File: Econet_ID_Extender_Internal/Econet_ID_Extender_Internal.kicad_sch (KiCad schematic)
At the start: 3 parts, among them J1 Conn_01x03_Male, J2 Conn_02x08_Odd_Even, J3 Conn_02x06_Odd_Even

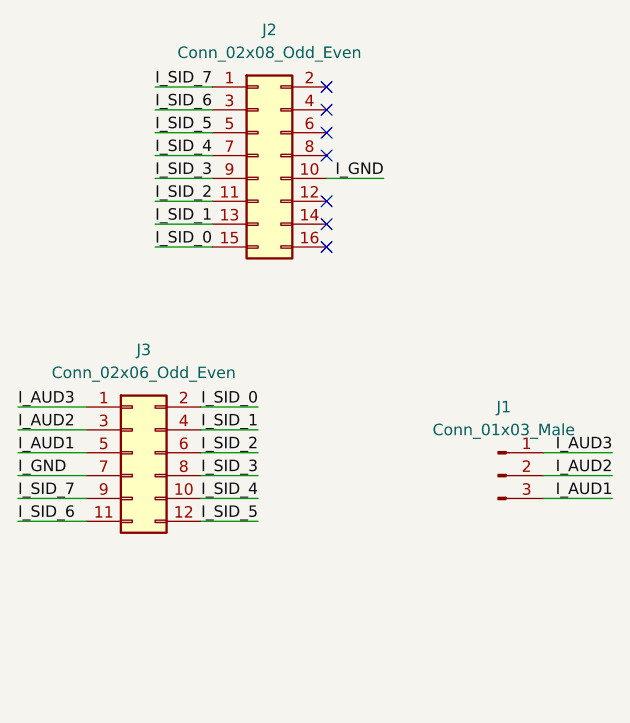
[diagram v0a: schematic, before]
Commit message: Swap to standard 2.54 pitch ribbon
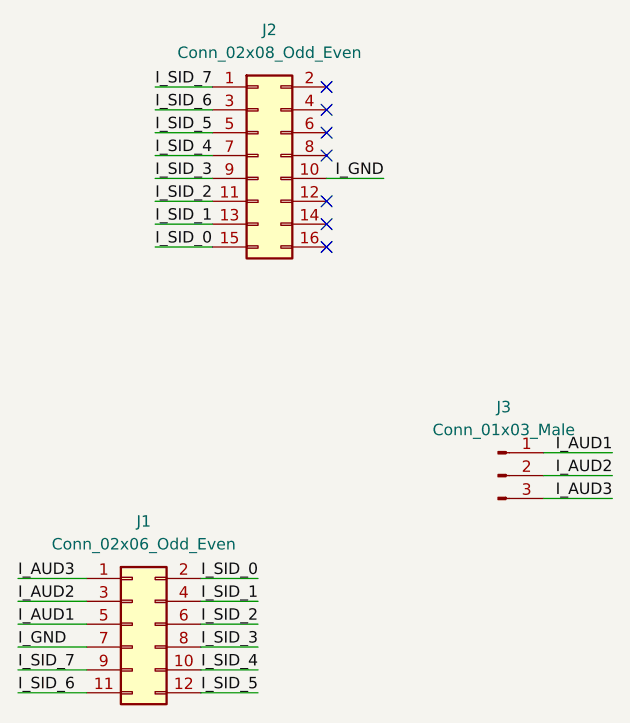
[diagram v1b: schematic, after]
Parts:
- removed J3: Conn_02x06_Odd_Even, AliExpress_Stuff:MicroMatch-12p-SMD, symbol Connector_Generic:Conn_02x06_Odd_Even
- added J1: Conn_02x06_Odd_Even, Connector_IDC:IDC-Header_2x06_P2.54mm_Vertical_SMD, symbol Connector_Generic:Conn_02x06_Odd_Even
- renumbered J1 to J3
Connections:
- net I_AUD1: now also J3.1 (Pin_1), J1.5 (Pin_5); no longer J3.3 (Pin_3)
- net I_AUD2: now also J1.3 (Pin_3)
- net I_AUD3: now also J3.3 (Pin_3), J1.1 (Pin_1); no longer J3.1 (Pin_1)
- net I_GND: now also J1.7 (Pin_7)
- net I_SID_0: now also J1.2 (Pin_2)
- net I_SID_1: now also J1.4 (Pin_4)
- net I_SID_2: now also J1.6 (Pin_6)
- net I_SID_3: now also J1.8 (Pin_8)
- net I_SID_4: now also J1.10 (Pin_10)
- net I_SID_5: now also J1.12 (Pin_12)
- net I_SID_6: now also J1.11 (Pin_11)
- net I_SID_7: now also J1.9 (Pin_9)
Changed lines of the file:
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@@
+    (stroke (width 0) (type default) (color 0 0 0 0))
+  )
+  (wire (pts (xy 124.46 121.92) (xy 130.81 121.92))
     (stroke (width 0) (type default) (color 0 0 0 0))
   )
@@
     (stroke (width 0) (type default) (color 0 0 0 0))
   )
-  (wire (pts (xy 124.46 105.41) (xy 130.81 105.41))
-    (stroke (width 0) (type default) (color 0 0 0 0))
-  )
-  (wire (pts (xy 124.46 110.49) (xy 130.81 110.49))
-    (stroke (width 0) (type default) (color 0 0 0 0))
-  )
-  (wire (pts (xy 124.46 115.57) (xy 130.81 115.57))
+  (wire (pts (xy 104.14 132.08) (xy 111.76 132.08))
+    (stroke (width 0) (type default) (color 0 0 0 0))
+  )
+  (wire (pts (xy 124.46 129.54) (xy 130.81 129.54))
     (stroke (width 0) (type default) (color 0 0 0 0))
   )
@@
     (stroke (width 0) (type default) (color 0 0 0 0))
   )
+  (wire (pts (xy 104.14 121.92) (xy 111.76 121.92))
+    (stroke (width 0) (type default) (color 0 0 0 0))
+  )
   (wire (pts (xy 162.56 107.95) (xy 170.18 107.95))
     (stroke (width 0) (type default) (color 0 0 0 0))
   )
-  (wire (pts (xy 104.14 115.57) (xy 111.76 115.57))
-    (stroke (width 0) (type default) (color 0 0 0 0))
-  )
   (wire (pts (xy 119.38 74.93) (xy 125.73 74.93))
     (stroke (width 0) (type default) (color 0 0 0 0))
@@
     (stroke (width 0) (type default) (color 0 0 0 0))
   )
-  (wire (pts (xy 104.14 113.03) (xy 111.76 113.03))
-    (stroke (width 0) (type default) (color 0 0 0 0))
-  )
-  (wire (pts (xy 124.46 102.87) (xy 130.81 102.87))
+  (wire (pts (xy 124.46 134.62) (xy 130.81 134.62))
+    (stroke (width 0) (type default) (color 0 0 0 0))
+  )
+  (wire (pts (xy 104.14 127) (xy 111.76 127))
+    (stroke (width 0) (type default) (color 0 0 0 0))
+  )
+  (wire (pts (xy 124.46 124.46) (xy 130.81 124.46))
     (stroke (width 0) (type default) (color 0 0 0 0))
   )
@@
     (stroke (width 0) (type default) (color 0 0 0 0))
   )
-  (wire (pts (xy 124.46 113.03) (xy 130.81 113.03))
-    (stroke (width 0) (type default) (color 0 0 0 0))
-  )
-  (wire (pts (xy 104.14 102.87) (xy 111.76 102.87))
-    (stroke (width 0) (type default) (color 0 0 0 0))
-  )
   (wire (pts (xy 119.38 69.85) (xy 125.73 69.85))
     (stroke (width 0) (type default) (color 0 0 0 0))
@@
     (stroke (width 0) (type default) (color 0 0 0 0))
   )
-  (wire (pts (xy 104.14 105.41) (xy 111.76 105.41))
-    (stroke (width 0) (type default) (color 0 0 0 0))
-  )
-  (wire (pts (xy 104.14 107.95) (xy 111.76 107.95))
-    (stroke (width 0) (type default) (color 0 0 0 0))
-  )
-  (wire (pts (xy 104.14 110.49) (xy 111.76 110.49))
-    (stroke (width 0) (type default) (color 0 0 0 0))
-  )
-  (wire (pts (xy 124.46 107.95) (xy 130.81 107.95))
-    (stroke (width 0) (type default) (color 0 0 0 0))
-  )
-  (label "I_SID_4" (at 130.81 113.03 180)
-    (effects (font (size 1.27 1.27)) (justify right bottom))
+  (wire (pts (xy 124.46 127) (xy 130.81 127))
+    (stroke (width 0) (type default) (color 0 0 0 0))
+  )
+  (wire (pts (xy 124.46 132.08) (xy 130.81 132.08))
+    (stroke (width 0) (type default) (color 0 0 0 0))
+  )
+  (wire (pts (xy 104.14 134.62) (xy 111.76 134.62))
+    (stroke (width 0) (type default) (color 0 0 0 0))
+  )
+  (wire (pts (xy 104.14 124.46) (xy 111.76 124.46))
+    (stroke (width 0) (type default) (color 0 0 0 0))
+  )
+  (wire (pts (xy 104.14 129.54) (xy 111.76 129.54))
+    (stroke (width 0) (type default) (color 0 0 0 0))
   )
   (label "I_AUD2" (at 170.18 110.49 180)
     (effects (font (size 1.27 1.27)) (justify right bottom))
   )
-  (label "I_SID_1" (at 130.81 105.41 180)
-    (effects (font (size 1.27 1.27)) (justify right bottom))
-  )
-  (label "I_GND" (at 104.14 110.49 0)
-    (effects (font (size 1.27 1.27)) (justify left bottom))
-  )
-  (label "I_AUD1" (at 104.14 107.95 0)
-    (effects (font (size 1.27 1.27)) (justify left bottom))
+  (label "I_AUD2" (at 104.14 124.46 0)
+    (effects (font (size 1.27 1.27)) (justify left bottom))
+  )
+  (label "I_SID_3" (at 130.81 129.54 180)
+    (effects (font (size 1.27 1.27)) (justify right bottom))
   )
   (label "I_SID_3" (at 119.38 77.47 0)
     (effects (font (size 1.27 1.27)) (justify left bottom))
   )
-  (label "I_SID_3" (at 130.81 110.49 180)
-    (effects (font (size 1.27 1.27)) (justify right bottom))
-  )
-  (label "I_AUD3" (at 104.14 102.87 0)
-    (effects (font (size 1.27 1.27)) (justify left bottom))
-  )
-  (label "I_AUD2" (at 104.14 105.41 0)
-    (effects (font (size 1.27 1.27)) (justify left bottom))
-  )
-  (label "I_SID_2" (at 130.81 107.95 180)
-    (effects (font (size 1.27 1.27)) (justify right bottom))
-  )
-  (label "I_AUD1" (at 170.18 113.03 180)
-    (effects (font (size 1.27 1.27)) (justify right bottom))
-  )
-  (label "I_SID_7" (at 104.14 113.03 0)
-    (effects (font (size 1.27 1.27)) (justify left bottom))
+  (label "I_AUD3" (at 104.14 121.92 0)
+    (effects (font (size 1.27 1.27)) (justify left bottom))
+  )
+  (label "I_SID_7" (at 104.14 132.08 0)
+    (effects (font (size 1.27 1.27)) (justify left bottom))
+  )
+  (label "I_SID_4" (at 130.81 132.08 180)
+    (effects (font (size 1.27 1.27)) (justify right bottom))
+  )
+  (label "I_SID_2" (at 130.81 127 180)
+    (effects (font (size 1.27 1.27)) (justify right bottom))
+  )
+  (label "I_AUD3" (at 170.18 113.03 180)
+    (effects (font (size 1.27 1.27)) (justify right bottom))
   )
   (label "I_SID_1" (at 119.38 82.55 0)
@@
     (effects (font (size 1.27 1.27)) (justify left bottom))
   )
-  (label "I_SID_5" (at 130.81 115.57 180)
-    (effects (font (size 1.27 1.27)) (justify right bottom))
-  )
-  (label "I_SID_0" (at 130.81 102.87 180)
-    (effects (font (size 1.27 1.27)) (justify right bottom))
-  )
-  (label "I_SID_6" (at 104.14 115.57 0)
-    (effects (font (size 1.27 1.27)) (justify left bottom))
+  (label "I_SID_6" (at 104.14 134.62 0)
+    (effects (font (size 1.27 1.27)) (justify left bottom))
+  )
+  (label "I_SID_5" (at 130.81 134.62 180)
+    (effects (font (size 1.27 1.27)) (justify right bottom))
+  )
+  (label "I_SID_1" (at 130.81 124.46 180)
+    (effects (font (size 1.27 1.27)) (justify right bottom))
   )
   (label "I_SID_6" (at 119.38 69.85 0)
@@
     (effects (font (size 1.27 1.27)) (justify left bottom))
   )
+  (label "I_GND" (at 104.14 129.54 0)
+    (effects (font (size 1.27 1.27)) (justify left bottom))
+  )
   (label "I_GND" (at 144.78 77.47 180)
     (effects (font (size 1.27 1.27)) (justify right bottom))
   )
-  (label "I_AUD3" (at 170.18 107.95 180)
+  (label "I_AUD1" (at 170.18 107.95 180)
     (effects (font (size 1.27 1.27)) (justify right bottom))
   )
@@
     (effects (font (size 1.27 1.27)) (justify left bottom))
   )
-  (symbol (lib_id "Connector_Generic:Conn_02x06_Odd_Even") (at 116.84 107.95 0) (unit 1)
+  (label "I_AUD1" (at 104.14 127 0)
+    (effects (font (size 1.27 1.27)) (justify left bottom))
+  )
+  (label "I_SID_0" (at 130.81 121.92 180)
+    (effects (font (size 1.27 1.27)) (justify right bottom))
+  )
+  (symbol (lib_id "Connector_Generic:Conn_02x06_Odd_Even") (at 116.84 127 0) (unit 1)
     (in_bom yes) (on_board yes) (fields_autoplaced)
-    (property "Reference" "J3" (id 0) (at 118.11 96.52 0))
-    (property "Value" "Conn_02x06_Odd_Even" (id 1) (at 118.11 99.06 0))
-    (property "Footprint" "AliExpress_Stuff:MicroMatch-12p-SMD" (id 2) (at 116.84 107.95 0)
-      (effects (font (size 1.27 1.27)) hide)
-    )
-    (property "Datasheet" "~" (id 3) (at 116.84 107.95 0)
+    (property "Reference" "J1" (id 0) (at 118.11 115.57 0))
+    (property "Value" "Conn_02x06_Odd_Even" (id 1) (at 118.11 118.11 0))
+    (property "Footprint" "Connector_IDC:IDC-Header_2x06_P2.54mm_Vertical_SMD" (id 2) (at 116.84 127 0)
+      (effects (font (size 1.27 1.27)) hide)
+    )
+    (property "Datasheet" "~" (id 3) (at 116.84 127 0)
       (effects (font (size 1.27 1.27)) hide)
     )
@@
   (symbol (lib_id "Connector:Conn_01x03_Male") (at 157.48 110.49 0) (unit 1)
     (in_bom yes) (on_board yes) (fields_autoplaced)
-    (property "Reference" "J1" (id 0) (at 158.115 102.87 0))
+    (property "Reference" "J3" (id 0) (at 158.115 102.87 0))
     (property "Value" "Conn_01x03_Male" (id 1) (at 158.115 105.41 0))
     (property "Footprint" "Connector_PinHeader_2.54mm:PinHeader_1x03_P2.54mm_Horizontal" (id 2) (at 157.48 110.49 0)
@@
   )
   (symbol_instances
-    (path "/6de08b45-c2eb-425e-969a-a2ca0ee9d278"
-      (reference "J1") (unit 1) (value "Conn_01x03_Male") (footprint "Connector_PinHeader_2.54mm:PinHeader_1x03_P2.54mm_Horizontal")
+    (path "/586dc93e-5bd2-4769-809e-60879a719e0c"
+      (reference "J1") (unit 1) (value "Conn_02x06_Odd_Even") (footprint "Connector_IDC:IDC-Header_2x06_P2.54mm_Vertical_SMD")
     )
     (path "/f5a51d67-d4d8-4a20-9f32-4740415aeda5"
       (reference "J2") (unit 1) (value "Conn_02x08_Odd_Even") (footprint "Connector_PinSocket_2.54mm:PinSocket_2x08_P2.54mm_Vertical_SMD")
     )
-    (path "/2f14c702-6c32-4c2d-9f99-283f6a39b626"
-      (reference "J3") (unit 1) (value "Conn_02x06_Odd_Even") (footprint "AliExpress_Stuff:MicroMatch-12p-SMD")
-    )
-  )
+    (path "/6de08b45-c2eb-425e-969a-a2ca0ee9d278"
+      (reference "J3") (unit 1) (value "Conn_01x03_Male") (footprint "Connector_PinHeader_2.54mm:PinHeader_1x03_P2.54mm_Horizontal")
+    )
+  )
